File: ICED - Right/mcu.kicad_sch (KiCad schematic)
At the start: 48 parts, among them P1 Conn_ARM_JTAG_SWD_10, P2 DX07S024XJ1R1100, P3 CONN_17, P4 692121130100, P5 RGB Out, Q1 TC1264, U1 MK20DX256VLH7, X1 NX3225SA-16.000MHZ-STD-CSR-

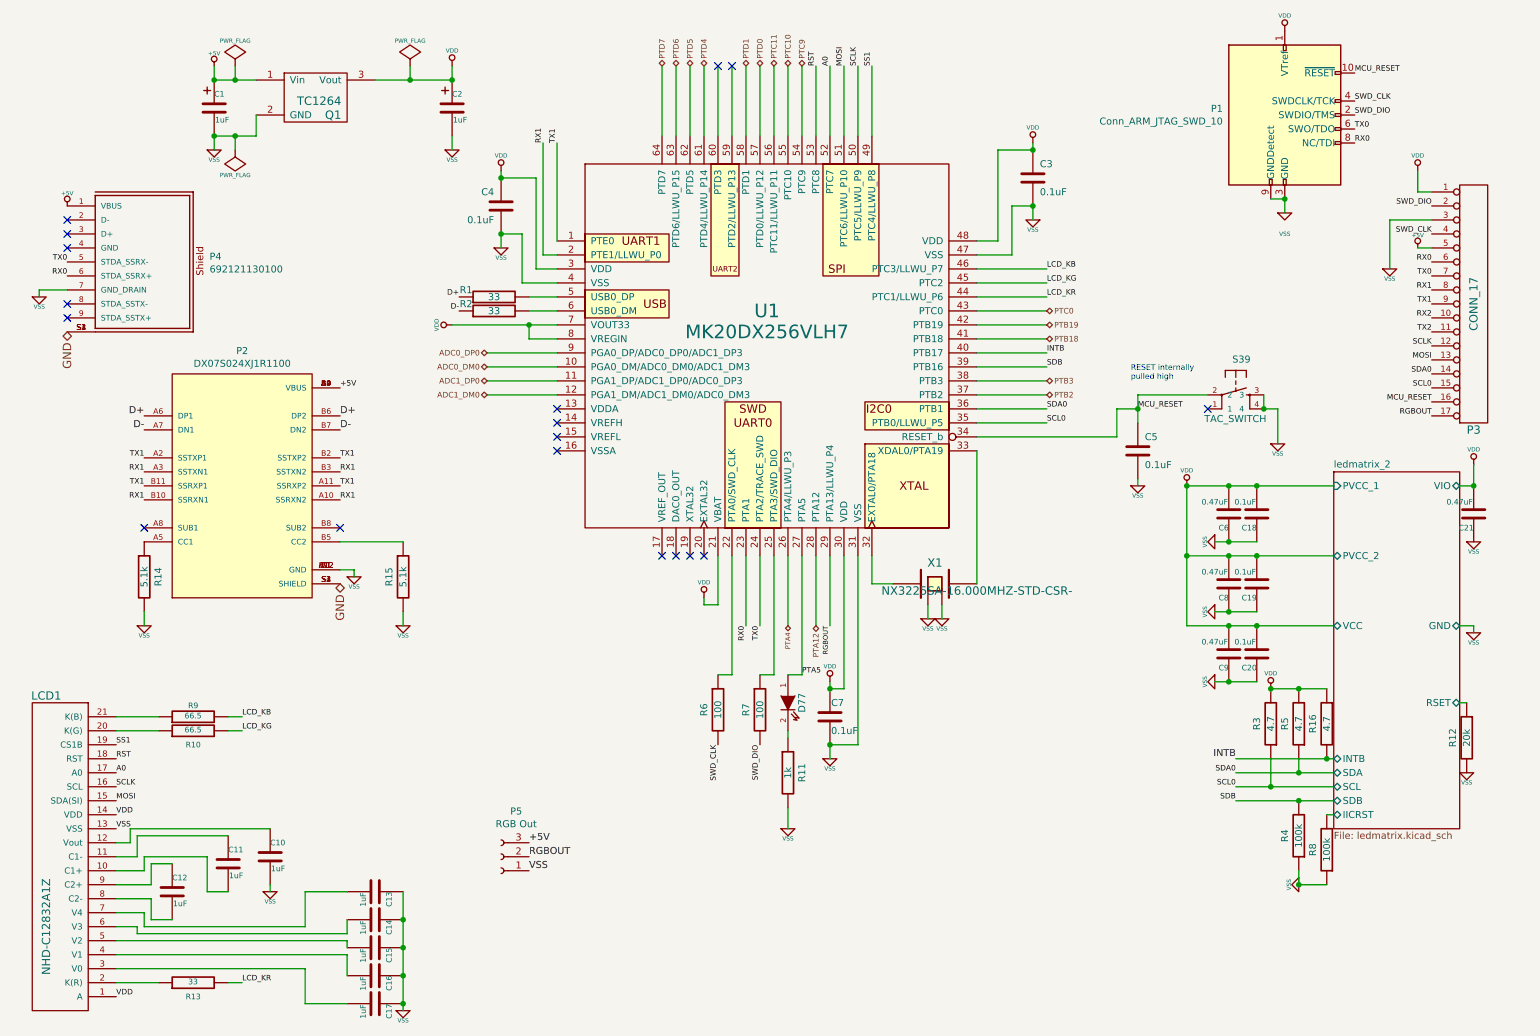
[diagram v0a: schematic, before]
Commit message: Upgrade project + Right changes
- Replace MXALPS sockets by Kailh Hot-swaps
- Replace the LED controller
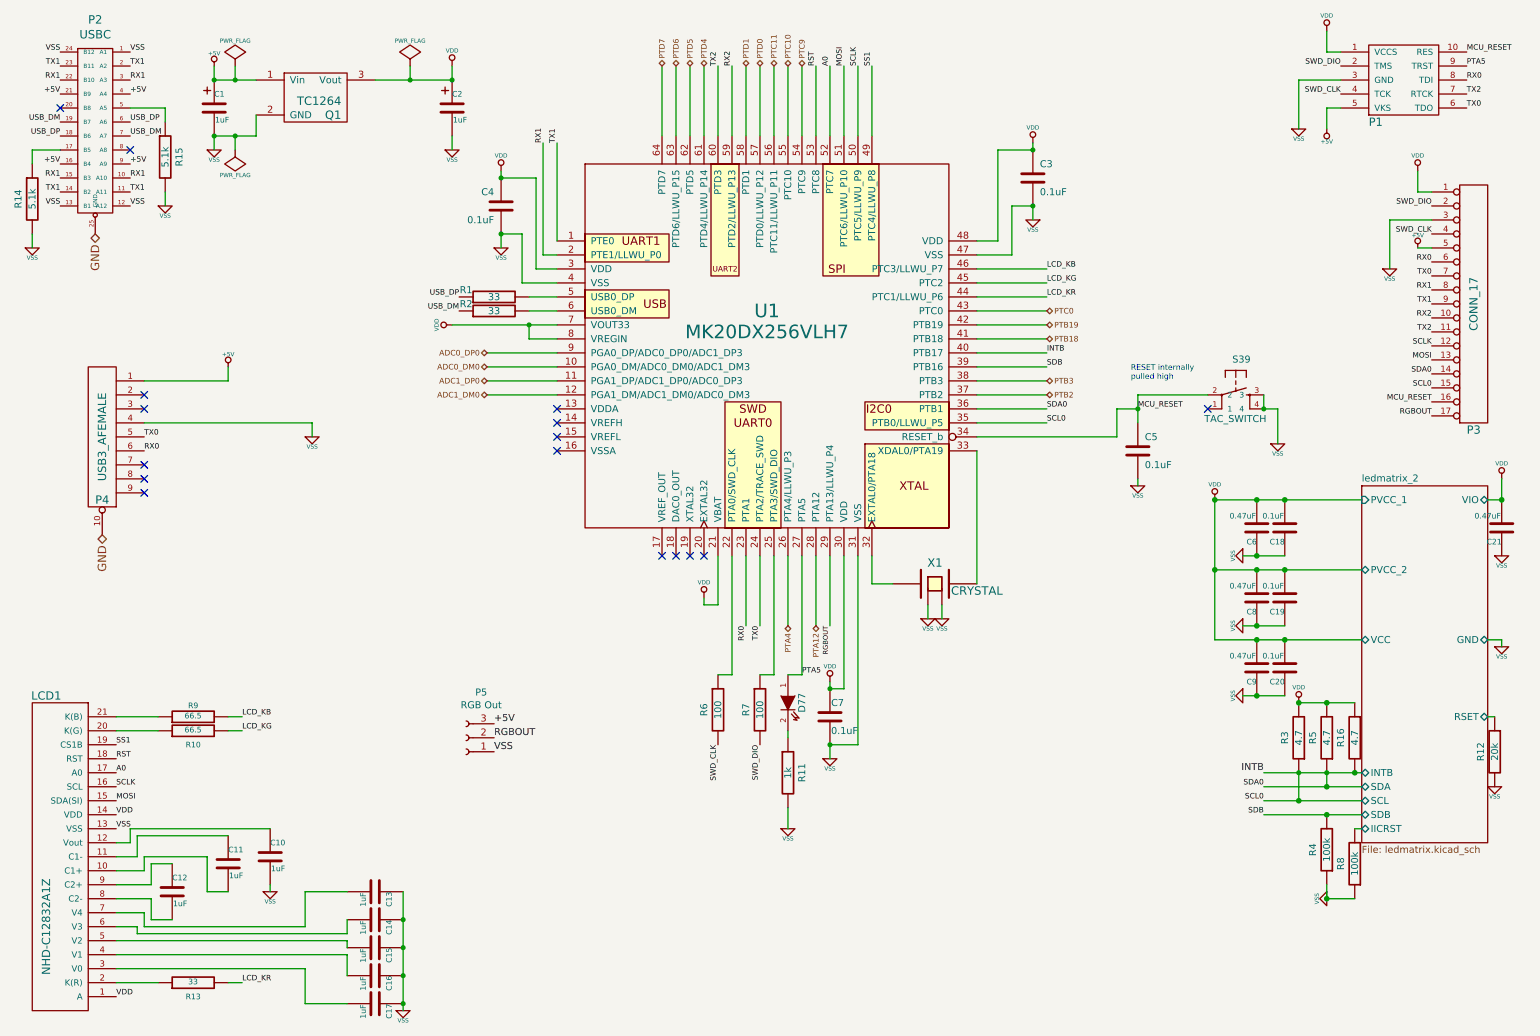
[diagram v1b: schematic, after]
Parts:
- removed P1: Conn_ARM_JTAG_SWD_10, prettylib:SHF-105-01-L-D-TH, symbol Connector:Conn_ARM_JTAG_SWD_10
- removed P2: DX07S024XJ1R1100, JAE_DX07S024XJ1R1100, symbol ICEDLeft:DX07S024XJ1R1100
- removed P4: 692121130100, 692121130100, symbol ICEDLeft:692121130100
- removed R14, R15: 5.1k, prettylib:SMD-1005, symbol ICEDLeft:R
- added P1: FLASH_HDR, prettylib:JLINK_NEEDLE, symbol ICEDRight:FLASH_HDR
- added P2: USBC, prettylib:USB_C_MIDMOUNT_TH_IMPCUT, symbol ICEDRight:USBC
- added P4: USB3_AFEMALE, prettylib:USB3_AFEMALE_MOD, symbol ICEDRight:USB3
- added R14, R15: 5.1k, prettylib:SMD-1005, symbol ICEDRight:R
- C1, C2: symbol ICEDLeft:CT -> ICEDRight:CT
- C10, C11, C12, C13, C14, C15, C16, C17, C3, C4, C5, C7: symbol ICEDLeft:C -> ICEDRight:C
- D77: symbol ICEDLeft:LED -> ICEDRight:LED
- LCD1: symbol ICEDLeft:NHD-C12832A1Z -> ICEDRight:NHD-C12832A1Z
- P3: symbol ICEDLeft:CONN_17 -> ICEDRight:CONN_17
- Q1: symbol ICEDLeft:TC1264 -> ICEDRight:TC1264
- R1, R10, R11, R13, R2, R6, R7, R9: symbol ICEDLeft:R -> ICEDRight:R
- S39: symbol ICEDLeft:TAC_SWITCH -> ICEDRight:TAC_SWITCH
- U1: symbol ICEDLeft:MK20DX256VLH7 -> ICEDRight:MK20DX256VLH7
- X1: value NX3225SA-16.000MHZ-STD-CSR- -> CRYSTAL; symbol ICEDLeft:CRYSTAL -> ICEDRight:CRYSTAL
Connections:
- net SCL0 is gone; now on net INTB: P3.15, R3.1, U1.35 (PTB0/LLWU_P5)
- net SDA0 is gone; now on net INTB: P3.14, R5.1, U1.36 (PTB1)
- net +5V: now also P1.5 (VKS), P2.16 (B4), P2.21 (B9), P2.4 (A4), P2.9 (A9), P4.1
- net GND: now also P2.25 (GND), P4.10
- net MCU_RESET: now also P1.10 (RES)
- net PTA5: now also P1.9 (TRST)
- net RX0: now also P1.8 (TDI), P4.6
- net RX1: now also P2.10 (A10), P2.15 (B3), P2.22 (B10), P2.3 (A3)
- net RX2: now also U1.59 (PTD2/LLWU_P13)
- net SWD_CLK: now also P1.4 (TCK)
- net SWD_DIO: now also P1.2 (TMS)
- net TX0: now also P1.6 (TDO), P4.5
- net TX1: now also P2.11 (A11), P2.14 (B2), P2.2 (A2), P2.23 (B11)
- net TX2: now also U1.60 (PTD3), P1.7 (RTCK)
- net VDD: now also P1.1 (VCCS)
- net VSS: now also P1.3 (GND), P2.1 (A1), P2.12 (A12), P2.13 (B1), P2.24 (B12), P4.4, R14.2, R15.2
- net D+ renamed USB_DP
- net USB_DP: now also P2.18 (B6), P2.6 (A6)
- net D- renamed USB_DM
- net USB_DM: now also P2.19 (B7), P2.7 (A7)
- new net: P2.17 (B5), R14.1
- new net: P2.5 (A5), R15.1
- no-connect marks 18 -> 16
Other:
- title: ICED-L -> ICED-R

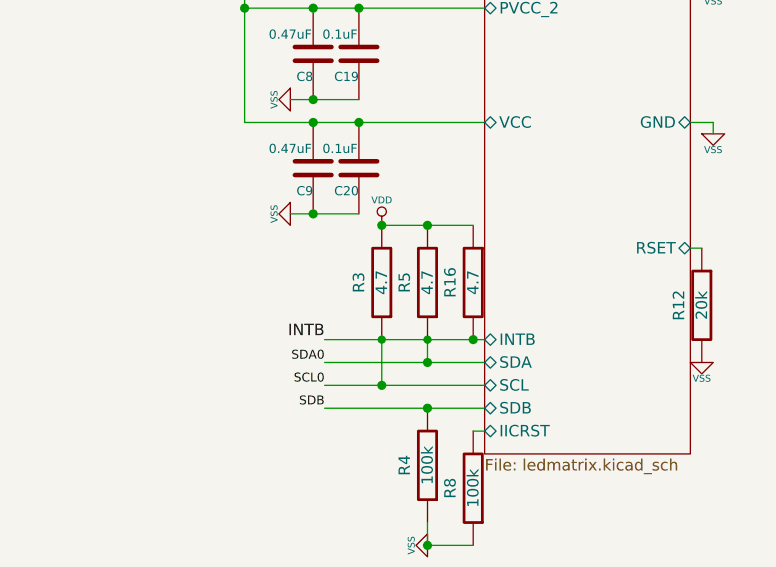
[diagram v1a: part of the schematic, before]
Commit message: Place all LEDs with their switch + resistors
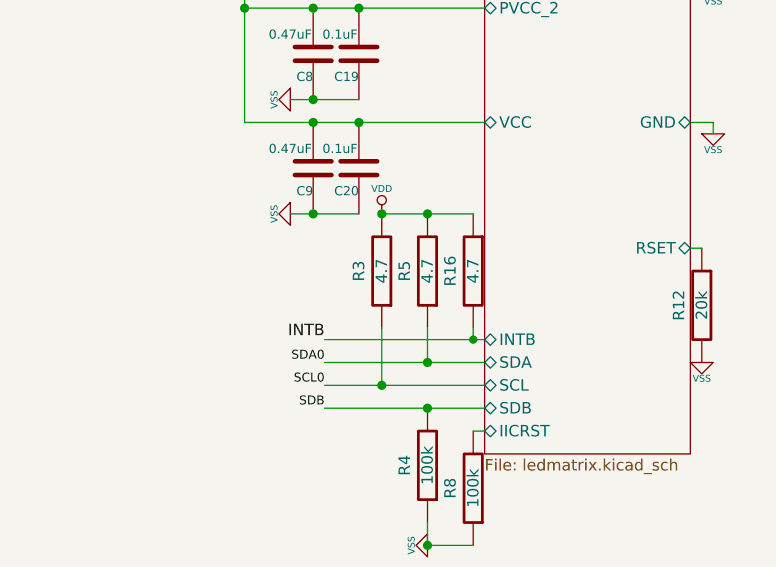
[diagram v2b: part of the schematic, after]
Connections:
- net INTB: no longer P3.14, P3.15, R3.1, R5.1, U1.35 (PTB0/LLWU_P5), U1.36 (PTB1)
- new net SCL0: P3.15, R3.1, U1.35 (PTB0/LLWU_P5)
- new net SDA0: P3.14, R5.1, U1.36 (PTB1)
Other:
- moved on the sheet: R16, R3, R5
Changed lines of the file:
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@@
   (junction (at 242.57 114.3) (diameter 1.016) (color 0 0 0 0))
   (junction (at 242.57 127) (diameter 1.016) (color 0 0 0 0))
-  (junction (at 245.11 138.43) (diameter 1.016) (color 0 0 0 0))
-  (junction (at 245.11 151.13) (diameter 0) (color 0 0 0 0))
+  (junction (at 245.11 137.16) (diameter 1.016) (color 0 0 0 0))
   (junction (at 245.11 156.21) (diameter 1.016) (color 0 0 0 0))
-  (junction (at 250.19 138.43) (diameter 1.016) (color 0 0 0 0))
-  (junction (at 250.19 151.13) (diameter 0) (color 0 0 0 0))
+  (junction (at 250.19 137.16) (diameter 1.016) (color 0 0 0 0))
   (junction (at 250.19 153.67) (diameter 1.016) (color 0 0 0 0))
   (junction (at 250.19 158.75) (diameter 1.016) (color 0 0 0 0))
   (junction (at 250.19 173.99) (diameter 1.016) (color 0 0 0 0))
-  (junction (at 255.27 151.13) (diameter 1.016) (color 0 0 0 0))
+  (junction (at 255.27 151.13) (diameter 0) (color 0 0 0 0))
   (junction (at 281.94 101.6) (diameter 1.016) (color 0 0 0 0))
   (no_connect (at 20.32 30.48))
@@
     (stroke (width 0) (type default) (color 0 0 0 0))
   )
-  (wire (pts (xy 238.76 151.13) (xy 245.11 151.13))
+  (wire (pts (xy 238.76 151.13) (xy 255.27 151.13))
     (stroke (width 0) (type solid) (color 0 0 0 0))
   )
@@
     (stroke (width 0) (type default) (color 0 0 0 0))
   )
-  (wire (pts (xy 245.11 151.13) (xy 245.11 156.21))
-    (stroke (width 0) (type solid) (color 0 0 0 0))
-  )
-  (wire (pts (xy 245.11 151.13) (xy 250.19 151.13))
+  (wire (pts (xy 245.11 149.86) (xy 245.11 156.21))
     (stroke (width 0) (type solid) (color 0 0 0 0))
   )
@@
     (stroke (width 0) (type default) (color 0 0 0 0))
   )
-  (wire (pts (xy 250.19 138.43) (xy 245.11 138.43))
-    (stroke (width 0) (type solid) (color 0 0 0 0))
-  )
-  (wire (pts (xy 250.19 138.43) (xy 255.27 138.43))
-    (stroke (width 0) (type solid) (color 0 0 0 0))
-  )
-  (wire (pts (xy 250.19 151.13) (xy 250.19 153.67))
-    (stroke (width 0) (type solid) (color 0 0 0 0))
-  )
-  (wire (pts (xy 250.19 151.13) (xy 255.27 151.13))
+  (wire (pts (xy 250.19 137.16) (xy 245.11 137.16))
+    (stroke (width 0) (type solid) (color 0 0 0 0))
+  )
+  (wire (pts (xy 250.19 137.16) (xy 255.27 137.16))
+    (stroke (width 0) (type solid) (color 0 0 0 0))
+  )
+  (wire (pts (xy 250.19 149.86) (xy 250.19 153.67))
     (stroke (width 0) (type solid) (color 0 0 0 0))
   )
@@
   )
   (wire (pts (xy 252.73 30.48) (xy 250.19 30.48))
+    (stroke (width 0) (type default) (color 0 0 0 0))
+  )
+  (wire (pts (xy 255.27 149.86) (xy 255.27 151.13))
     (stroke (width 0) (type default) (color 0 0 0 0))
   )
@@
     (pin "1")
   )
-  (symbol (lib_id "ICEDLeft:VDD") (at 245.11 138.43 0) (unit 1)
-    (in_bom yes) (on_board yes)
-    (property "Reference" "#PWR0108" (id 0) (at 245.11 135.89 0)
-      (effects (font (size 0.762 0.762)) hide)
-    )
-    (property "Value" "VDD" (id 1) (at 245.11 135.636 0)
-      (effects (font (size 0.762 0.762)))
-    )
-    (property "Footprint" "" (id 2) (at 245.11 138.43 0)
-      (effects (font (size 1.524 1.524)))
-    )
-    (property "Datasheet" "" (id 3) (at 245.11 138.43 0)
+  (symbol (lib_id "ICEDLeft:VDD") (at 245.11 137.16 0) (unit 1)
+    (in_bom yes) (on_board yes)
+    (property "Reference" "#PWR0108" (id 0) (at 245.11 134.62 0)
+      (effects (font (size 0.762 0.762)) hide)
+    )
+    (property "Value" "VDD" (id 1) (at 245.11 134.366 0)
+      (effects (font (size 0.762 0.762)))
+    )
+    (property "Footprint" "" (id 2) (at 245.11 137.16 0)
+      (effects (font (size 1.524 1.524)))
+    )
+    (property "Datasheet" "" (id 3) (at 245.11 137.16 0)
       (effects (font (size 1.524 1.524)))
     )
@@
     (pin "2")
   )
-  (symbol (lib_id "ICEDLeft:R") (at 245.11 144.78 180) (unit 1)
-    (in_bom yes) (on_board yes)
-    (property "Reference" "R3" (id 0) (at 242.57 144.78 90))
-    (property "Value" "4.7" (id 1) (at 245.11 144.78 90))
-    (property "Footprint" "prettylib:SMD-1005" (id 2) (at 247.65 144.78 90)
-      (effects (font (size 1.524 1.524)) hide)
-    )
-    (property "Datasheet" "" (id 3) (at 245.11 144.78 0)
+  (symbol (lib_id "ICEDLeft:R") (at 245.11 143.51 180) (unit 1)
+    (in_bom yes) (on_board yes)
+    (property "Reference" "R3" (id 0) (at 242.57 143.51 90))
+    (property "Value" "4.7" (id 1) (at 245.11 143.51 90))
+    (property "Footprint" "prettylib:SMD-1005" (id 2) (at 247.65 143.51 90)
+      (effects (font (size 1.524 1.524)) hide)
+    )
+    (property "Datasheet" "" (id 3) (at 245.11 143.51 0)
       (effects (font (size 1.524 1.524)) hide)
     )
@@
     (pin "2")
   )
-  (symbol (lib_id "ICEDLeft:R") (at 250.19 144.78 180) (unit 1)
-    (in_bom yes) (on_board yes)
-    (property "Reference" "R5" (id 0) (at 247.65 144.78 90))
-    (property "Value" "4.7" (id 1) (at 250.19 144.78 90))
-    (property "Footprint" "prettylib:SMD-1005" (id 2) (at 252.73 144.78 90)
-      (effects (font (size 1.524 1.524)) hide)
-    )
-    (property "Datasheet" "" (id 3) (at 250.19 144.78 0)
+  (symbol (lib_id "ICEDLeft:R") (at 250.19 143.51 180) (unit 1)
+    (in_bom yes) (on_board yes)
+    (property "Reference" "R5" (id 0) (at 247.65 143.51 90))
+    (property "Value" "4.7" (id 1) (at 250.19 143.51 90))
+    (property "Footprint" "prettylib:SMD-1005" (id 2) (at 252.73 143.51 90)
+      (effects (font (size 1.524 1.524)) hide)
+    )
+    (property "Datasheet" "" (id 3) (at 250.19 143.51 0)
       (effects (font (size 1.524 1.524)) hide)
     )
@@
     (pin "2")
   )
-  (symbol (lib_id "ICEDLeft:R") (at 255.27 144.78 0) (mirror y) (unit 1)
-    (in_bom yes) (on_board yes)
-    (property "Reference" "R16" (id 0) (at 252.73 144.78 90))
-    (property "Value" "4.7" (id 1) (at 255.27 144.78 90))
-    (property "Footprint" "prettylib:SMD-1005" (id 2) (at 257.81 144.78 90)
-      (effects (font (size 1.524 1.524)) hide)
-    )
-    (property "Datasheet" "" (id 3) (at 255.27 144.78 0)
-      (effects (font (size 1.524 1.524)) hide)
-    )
+  (symbol (lib_id "ICEDLeft:R") (at 255.27 143.51 0) (mirror y) (unit 1)
+    (in_bom yes) (on_board yes)
+    (property "Reference" "R16" (id 0) (at 252.73 143.51 90))
+    (property "Value" "4.7" (id 1) (at 255.27 143.51 90))
+    (property "Footprint" "prettylib:SMD-1005" (id 2) (at 257.81 143.51 90)
+      (effects (font (size 1.524 1.524)) hide)
+    )
+    (property "Datasheet" "" (id 3) (at 255.27 143.51 0)
+      (effects (font (size 1.524 1.524)) hide)
+    )
